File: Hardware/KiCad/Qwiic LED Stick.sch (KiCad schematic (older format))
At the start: 39 parts, among them J1 CONN_021X02_NO_SILK, J2 SMD, J3 PTH, J4 SMD, J5 CONN_041X04_NO_SILK, J6 AVR_SPI_PROG_3X2TESTPOINTS, U1 Tiny85-20-SMT

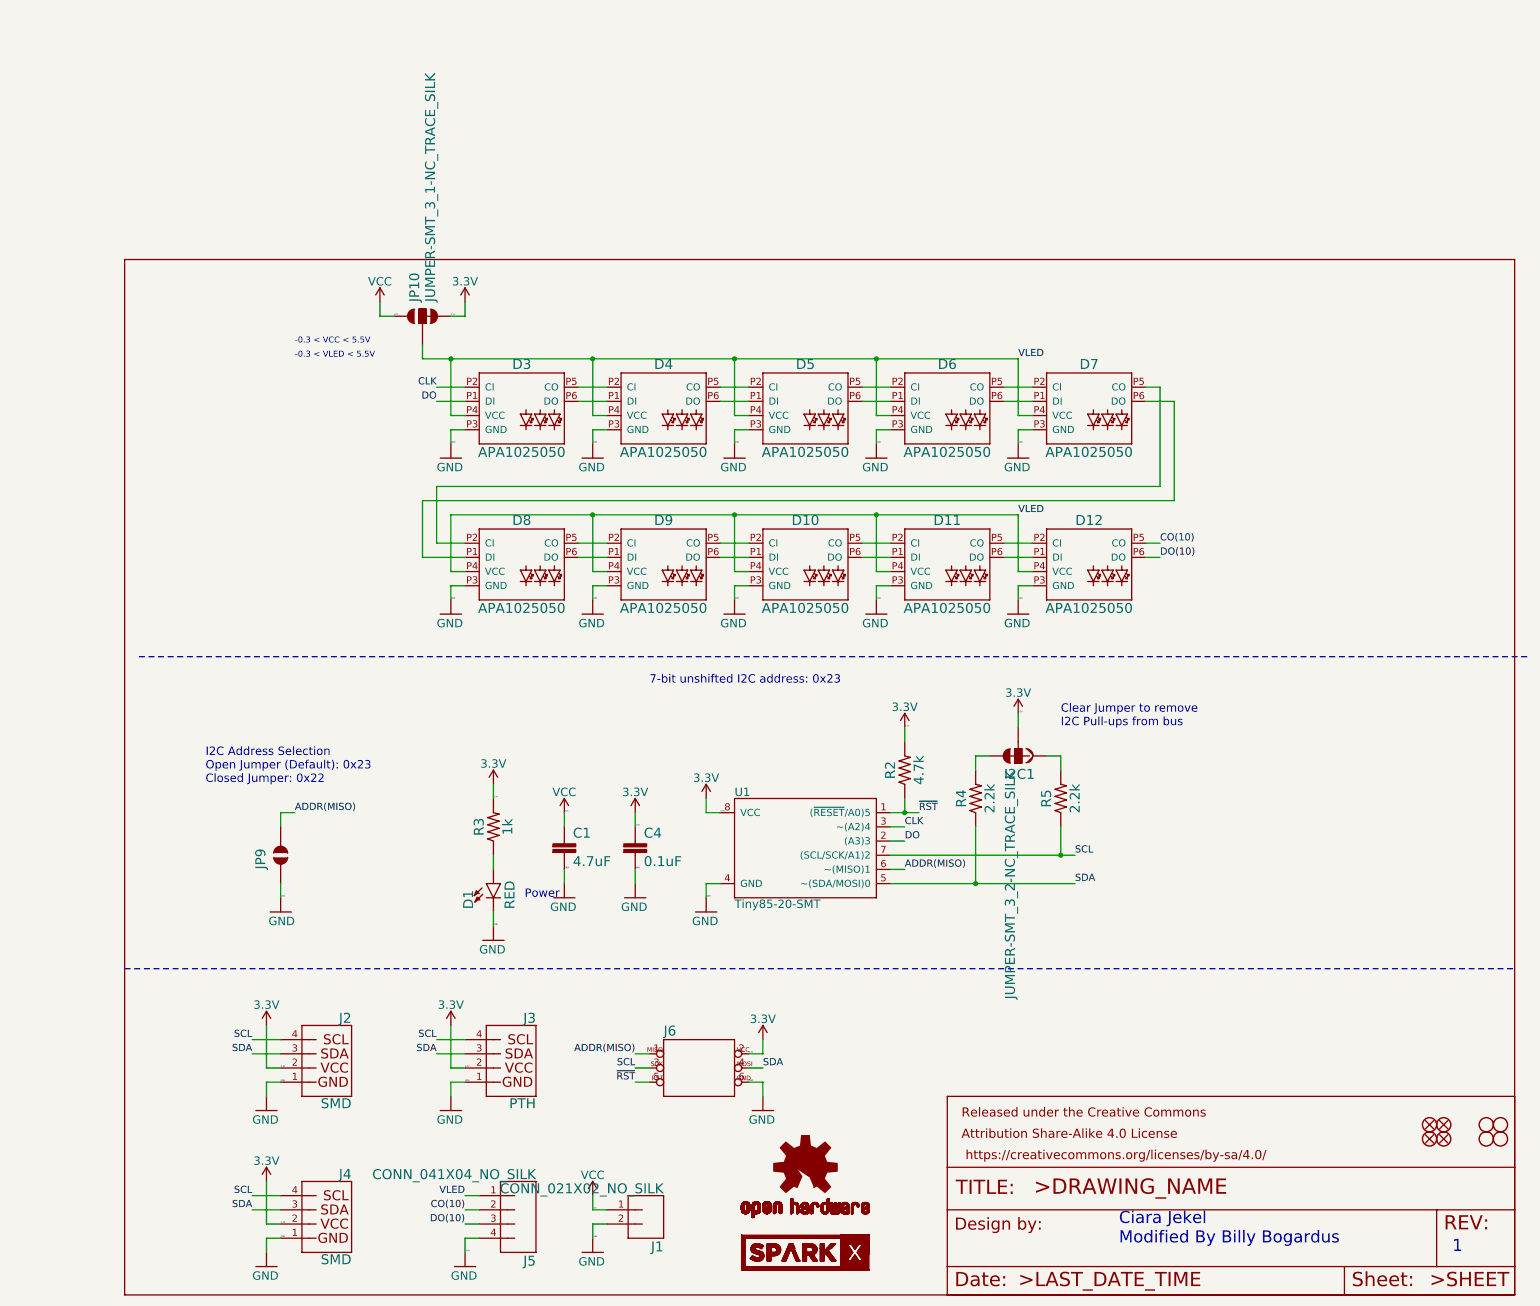
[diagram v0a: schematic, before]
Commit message: created a smaller Board
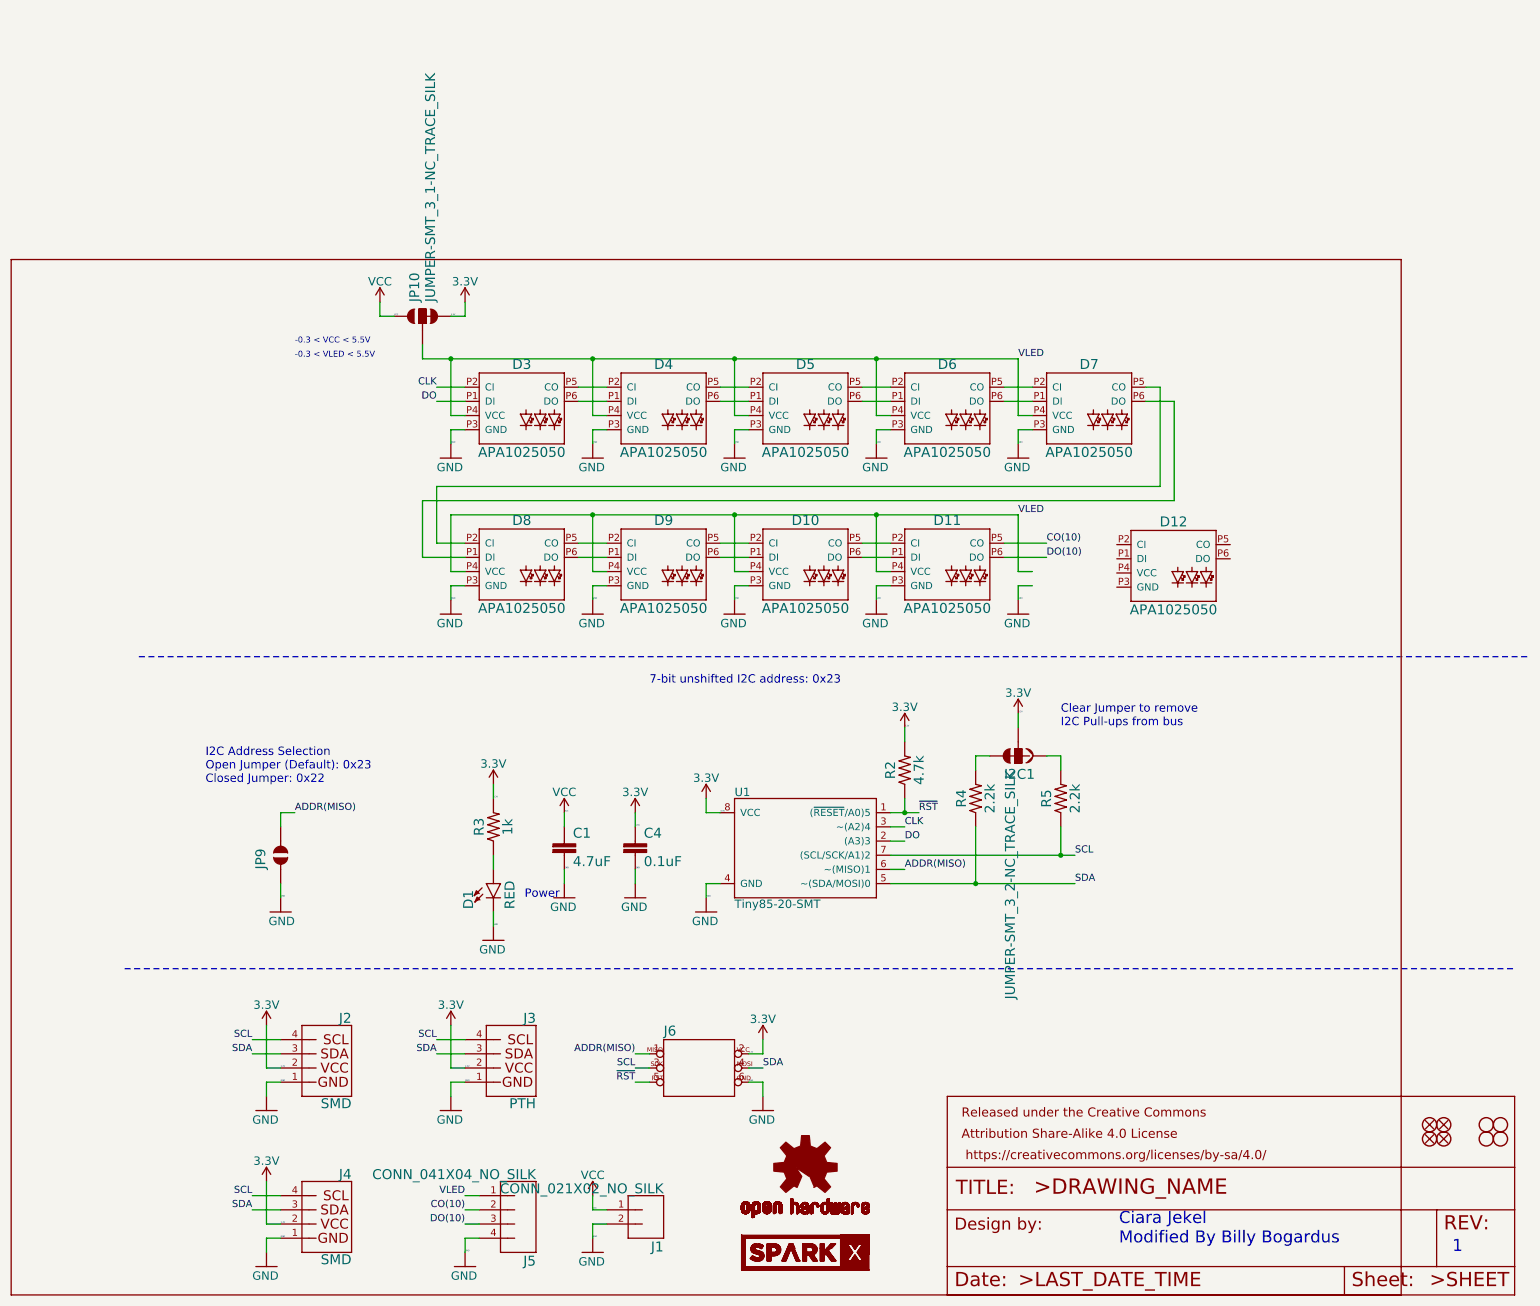
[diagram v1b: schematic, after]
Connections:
- net CO(10): now also D11.P5 (CO); no longer D12.P5 (CO)
- net DO(10): now also D11.P6 (DO); no longer D12.P6 (DO)
- net GND: no longer D12.P3 (GND)
- net VLED: no longer D12.P4 (VCC)
- net at D12.P2 (CI): no longer D11.P5 (CO)
- net at D12.P1 (DI): no longer D11.P6 (DO)
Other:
- moved on the sheet: D12
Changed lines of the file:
@@
 EESchema Schematic File Version 4
+LIBS:Qwiic LED Stick-cache
 EELAYER 30 0
 EELAYER END
@@
 DO
 Wire Wire Line
-	7500 4300 7300 4300
-Wire Wire Line
-	7300 4200 7500 4200
-Wire Wire Line
 	6500 4200 6300 4200
 Wire Wire Line
@@
 Text Label 3500 9000 2    50   ~ 0
 DO(10)
-Wire Wire Line
-	8300 4300 8400 4300
-Text Label 8400 4300 0    50   ~ 0
+Text Label 7600 4300 0    50   ~ 0
 DO(10)
-Wire Wire Line
-	8300 4200 8400 4200
-Text Label 8400 4200 0    50   ~ 0
+Text Label 7600 4200 0    50   ~ 0
 CO(10)
 Wire Wire Line
@@
 L Qwiic_LED_Stick-eagle-import:FRAME-LETTER FRAME1
 U 1 1 CC96BE83
-P 1100 9500
-F 0 "FRAME1" H 1100 9500 50  0001 C CNN
-F 1 "FRAME-LETTER" H 1100 9500 50  0001 C CNN
-F 2 "Qwiic LED Stick:CREATIVE_COMMONS" H 1100 9500 50  0001 C CNN
-F 3 "" H 1100 9500 50  0001 C CNN
-	1    1100 9500
+P 300 9500
+F 0 "FRAME1" H 300 9500 50  0001 C CNN
+F 1 "FRAME-LETTER" H 300 9500 50  0001 C CNN
+F 2 "Qwiic LED Stick:CREATIVE_COMMONS" H 300 9500 50  0001 C CNN
+F 3 "" H 300 9500 50  0001 C CNN
+	1    300  9500
 	1    0    0    -1
 $EndComp
@@
 L Qwiic_LED_Stick-eagle-import:APA1025050 D12
 U 1 1 B603868B
-P 7900 4300
-F 0 "D12" H 7900 4520 70  0000 C BNN
-F 1 "APA1025050" H 7900 3900 70  0000 C BNN
-F 2 "Qwiic LED Stick:APA102-5050" H 7900 4300 50  0001 C CNN
-F 3 "" H 7900 4300 50  0001 C CNN
-	1    7900 4300
+P 8495 4310
+F 0 "D12" H 8495 4530 70  0000 C BNN
+F 1 "APA1025050" H 8495 3910 70  0000 C BNN
+F 2 "Qwiic LED Stick:APA102-5050" H 8495 4310 50  0001 C CNN
+F 3 "" H 8495 4310 50  0001 C CNN
+	1    8495 4310
 	1    0    0    -1
 $EndComp
@@
 Text Notes 2300 2900 0    42   ~ 0
 -0.3 < VLED < 5.5V
+Wire Wire Line
+	7300 4300 7600 4300
+Wire Wire Line
+	7300 4200 7600 4200
 $EndSCHEMATC
